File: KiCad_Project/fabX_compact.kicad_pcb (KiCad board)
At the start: 2 copper layers, 140.9 x 101.6 mm, 68 parts, among them J1 Conn_02x15_Odd_Even, J3 Conn_02x07_Odd_Even, J4 Conn_01x06, J6 Conn_01x08, Q1 2N7002, Q2 AO3401A, Q3 2N7002, Q4 2N7002, Q5 BCX19, Q6 BCX19, U1 MCP23008, U2 MCP23008

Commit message: some PCB progress
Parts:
- added J5: Conn_02x07_Odd_Even, Connector_IDC:IDC-Header_2x07_P2.54mm_Horizontal, F.Cu at (140.9, 96.8)
- added K2: FINDER-36.11-4301, Relay_THT:Relay_SPST_TE_PCN-1xxD3MHZ, F.Cu at (177.3, 121.7)
- added R22: 10k, Resistor_SMD:R_0603_1608Metric, F.Cu at (155.5, 79.8)
- added R23: 10k, Resistor_SMD:R_0603_1608Metric, F.Cu at (144.3, 79.8)
- added R24: 10k, Resistor_SMD:R_0603_1608Metric, F.Cu at (144.3, 78.2)
- C2: value C -> 100n 6v3 X7R
- D1, R10, R11, R12, R13, R14, R15, R16, R19, R9: moved to F.Cu
- D2, D3, D4, D5: moved to B.Cu
- JP4, JP5, JP6: value SolderJumper_3_Open -> SolderJumper_2_Open; footprint Jumper:SolderJumper-3_P1.3mm_Open_Pad1.0x1.5mm_NumberLabels -> Jumper:SolderJumper-2_P1.3mm_Open_RoundedPad1.0x1.5mm
- moved R1 143.7 mm to (214.1, 99.0), turned to 90 degrees
- moved H2 143.6 mm to (213.3, 130.6)
- moved Q2 140.1 mm to (212.3, 87.6), turned to 0 degrees
- moved R5 140.1 mm to (208.9, 99.0), turned to -90 degrees
- moved Q1 140.0 mm to (211.5, 99.0), turned to 0 degrees
- moved H1 139.7 mm to (216.1, 118.8)
- moved Q3 138.6 mm to (208.7, 87.6), turned to 0 degrees
- moved R6 138.0 mm to (208.9, 90.2), turned to 180 degrees
- moved R7 136.2 mm to (208.9, 85.0), turned to 0 degrees
- moved R14 135.9 mm to (212.1, 90.2)
- moved R15 134.8 mm to (212.1, 85.0)
- moved R19 117.2 mm to (168.3, 127.0)
- moved D1 114.7 mm to (170.3, 123.4)
- moved H3 114.2 mm to (226.9, 87.2)
- moved R8 111.6 mm to (167.5, 124.6)
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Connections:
- C2 pad 2: 5V -> +3V3
- J1 pad 10: /NFC_CS -> /NFC_IRQ
- J1 pad 19: /NFC_RST -> /NFC_CS
- J1 pad 20: /NFC_IRQ -> /NFC_RST
- J3 pad 10: /Ch3 -> /Ch4
- J3 pad 11: /Ch4 -> /Ch3
- J3 pad 12: /Ch5 -> /Ch2
- J3 pad 13: /Ch6 -> /Ch1
- J3 pad 14: /Ch7 -> /Ch0
- J3 pad 7: /Ch0 -> /Ch7
- J3 pad 8: /Ch1 -> /Ch6
- J3 pad 9: /Ch2 -> /Ch5
- JP4 pad 2: Net-(JP4-Pad2) -> Net-(U2-Pad5)
- JP5 pad 1: 5V -> GND
- JP6 pad 2: Net-(JP6-Pad2) -> Net-(U2-Pad3)
- U2 pad 12: In1 -> /Ch10
- U2 pad 13: In2 -> /Ch11
- U2 pad 14: In3 -> /Ch12
- U2 pad 15: In4 -> /Ch13
- U2 pad 16: In5 -> /Ch14
- U2 pad 17: In6 -> /Ch15
- U2 pad 18: In7 -> /Ch16
- U2 pad 19: unconnected-(U2-Pad19) -> /Ch17
- U2 pad 20: 5V -> +3V3
- U2 pad 3: Net-(JP4-Pad2) -> Net-(U2-Pad3)
- U2 pad 5: Net-(JP6-Pad2) -> Net-(U2-Pad5)
- U2 pad 6: 5V -> +3V3
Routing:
- net /NFC_CS: track 0.00 -> 86.7 mm, vias 0 -> 1
- net RX: track 20.0 -> 95.5 mm
- net TX: track 25.3 -> 88.8 mm
- net /coreRST: track 3.23 -> 65.4 mm, vias 0 -> 1
- net /COPI: track 17.7 -> 76.2 mm
- net /CIPO: track 19.0 -> 73.7 mm
- net /Fet1: track 53.8 -> 0.00 mm, vias 1 -> 0
- net GND: track 124.3 -> 72.0 mm, vias 9 -> 4
- net /SCLK: track 30.9 -> 82.0 mm
- net 3,3V: track 50.7 -> 0.00 mm
- net +3V3: track 35.4 -> 83.0 mm, vias 5 -> 0
- net /NFC_RST: track 36.9 -> 81.8 mm
- net /G0(BOOT): track 20.4 -> 57.6 mm, vias 2 -> 0
- net Net-(J6-Pad3): track 39.7 -> 2.59 mm
- net +5V: track 13.0 -> 49.5 mm, vias 2 -> 0
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- removed copper zone on B.Cu, net 5V
- removed copper zone on F.Cu, net GND
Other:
- board size 140.9 x 101.6 mm -> 62 x 90 mm
- board text removed: "3,3V, OUT4, OUT3, OUT2, OUT1 3,3V, GND, GND, GND, GND"
- board text removed: "5V"
- board text removed: "5V, OUT5, OUT6, OUT7, OUT8 5V, GND, GND, GND, GND"
- board text removed: ">"
- board text removed: "GND, IN7, IN5, IN3, IN1 GND, GND, IN6, IN4, IN2"
- board text removed: "MOSI, MISO, CLK, GND 3,3V, IO2, IO5, IO3"

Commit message: PCB progress
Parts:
- removed H1, H2: MountingHole_Pad, TestPoint:TestPoint_Loop_D2.50mm_Drill1.85mm
- removed kibuzzard-632A463E: G***, kibuzzard-632A463E
- removed kibuzzard-632A464C: G***, kibuzzard-632A464C
- removed kibuzzard-632A4658: G***, kibuzzard-632A4658
- removed kibuzzard-632A4688: G***, kibuzzard-632A4688
- removed kibuzzard-632A4693: G***, kibuzzard-632A4693
- removed kibuzzard-632A469F: G***, kibuzzard-632A469F
- added X2: Screw_Terminal_01x08, Connector_Phoenix_MSTB:PhoenixContact_MSTBA_2,5_8-G-5,08_1x08_P5.08mm_Horizontal, B.Cu at (167.7, 142.3)
- added kibuzzard-635FD364: G***, kibuzzard-635FD364, F.Cu at (128.0, 96.8)
- added kibuzzard-635FD36E: G***, kibuzzard-635FD36E, F.Cu at (128.0, 94.3)
- added kibuzzard-635FD378: G***, kibuzzard-635FD378, F.Cu at (128.0, 91.7)
- D2, D3, D4, D5: footprint LED_SMD:LED_0603_1608Metric -> LED_SMD:LED_1206_3216Metric_ReverseMount_Hole1.8x2.4mm; moved to F.Cu
- H10, H12, H13, H4, H6, H7: footprint MountingHole:MountingHole_3.2mm_M3 -> ownCon:MountingHole_3.2mm_M3_noSolder
- H11, H5, H8, H9: footprint MountingHole:MountingHole_3.2mm_M3 -> ownCon:MountingHole_3.2mm_M3_noSolderCorner
- K2: moved to B.Cu
- R16, R19: footprint Resistor_SMD:R_0603_1608Metric -> Resistor_SMD:R_2010_5025Metric
- moved H3 80.6 mm to (159.5, 131.4)
- moved R1 76.7 mm to (148.3, 138.5), turned to 0 degrees
- moved R14 75.2 mm to (154.4, 138.5)
- moved R6 75.1 mm to (151.3, 138.5)
- moved R7 74.7 mm to (151.9, 133.3)
- moved Q2 74.5 mm to (155.6, 135.9)
- moved Q3 74.5 mm to (152.0, 135.9)
- moved R15 74.5 mm to (155.4, 133.3)
- moved Q1 73.0 mm to (148.5, 135.9)
- moved R5 69.7 mm to (148.2, 133.3), turned to 0 degrees
- moved R9 55.6 mm to (125.5, 143.4), turned to 180 degrees
- moved D5 55.0 mm to (178.3, 119.5)
- moved R10 51.9 mm to (125.5, 140.0), turned to 180 degrees
- moved R12 48.3 mm to (125.5, 136.6), turned to 180 degrees
- moved R13 38.5 mm to (174.3, 120.2), turned to 0 degrees
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- renumbered JP1 to J1, JP2 to J2, JP3 to J3, JP4 to J4, JP5 to J5, JP6 to J6, J1 to X1, J3 to X3, J4 to X4, J5 to X5, J6 to X6
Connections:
- K2 pad 1: (no net) -> /Fet0
- K2 pad 2: (no net) -> +5V
- K2 pad 3: (no net) -> /Relay_COM
- K2 pad 4: (no net) -> /Relay_NO
- X4 pad 3: 3,3V -> +3V3
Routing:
- net +3V3: track 83.0 -> 219.6 mm, vias 0 -> 5
- net +5V: track 49.5 -> 169.0 mm
- net /Ch0: track 11.3 -> 116.1 mm, vias 0 -> 2
- net /Ch1: track 12.6 -> 100.0 mm, vias 0 -> 2
- net /Ch2: track 21.3 -> 98.2 mm, vias 0 -> 2
- net GND: track 72.0 -> 0.00 mm, vias 4 -> 28
- net /Relay_NO: track 0.00 -> 25.8 mm
- net /Fet0: track 0.00 -> 24.8 mm
- net /Relay_COM: track 0.00 -> 17.3 mm
- net /V_HIGH: track 0.00 -> 12.6 mm
- net /Fet2: track 0.00 -> 11.8 mm
- net /highOut: track 0.00 -> 9.79 mm
- net /Fet1: track 0.00 -> 7.09 mm
- net RX: track 95.5 -> 89.8 mm
- net TX: track 88.8 -> 83.4 mm
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- added copper zone on B.Cu, net GND
- added copper zone on F.Cu, net GND
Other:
- outline, holes or cut-outs redrawn
- board text added: "+3V3"
- board text added: "+5V"
- board text added: "COM"
- board text added: "CTS"
- board text added: "Ch. 0-7"
- board text added: "Ch. 10-17"
- board text added: "Ch0"
- board text added: "Ch1"
- board text added: "Ch2"
- board text added: "DTR"
- board text added: "GND"
- board text added: "LOut"
- board text added: "NO"
- board text added: "Nylon Screw only"
- board text added: "PWR"
- board text added: "RX"
- board text added: "TX"
- board text added: "V- High"
- board text added: "fabX FabLab München compact V0.1 @tinyledmatrix 2022-10-24"
- board text added: "hOut"
- board text removed: "fabX FabLab München compact V0.1 @tinyledmatrix 2022-09-21"

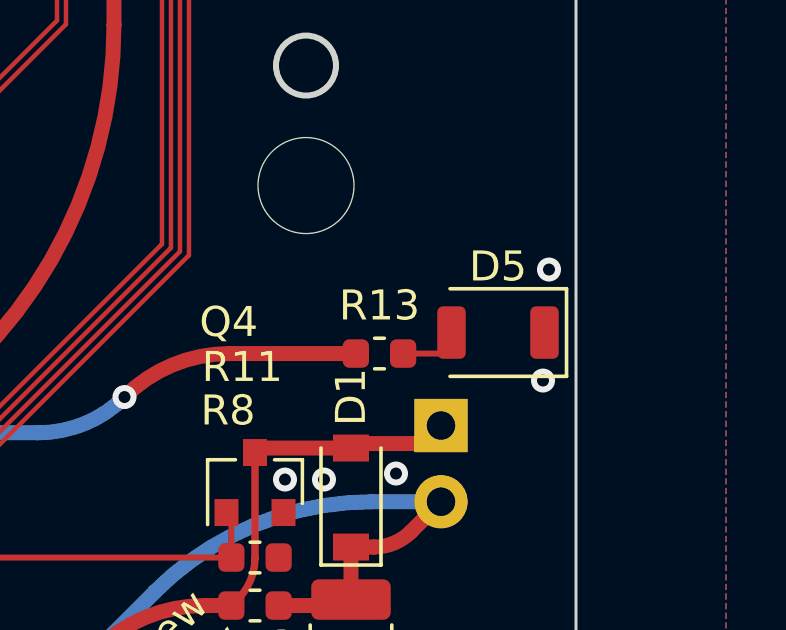
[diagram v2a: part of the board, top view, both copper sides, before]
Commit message: added bom
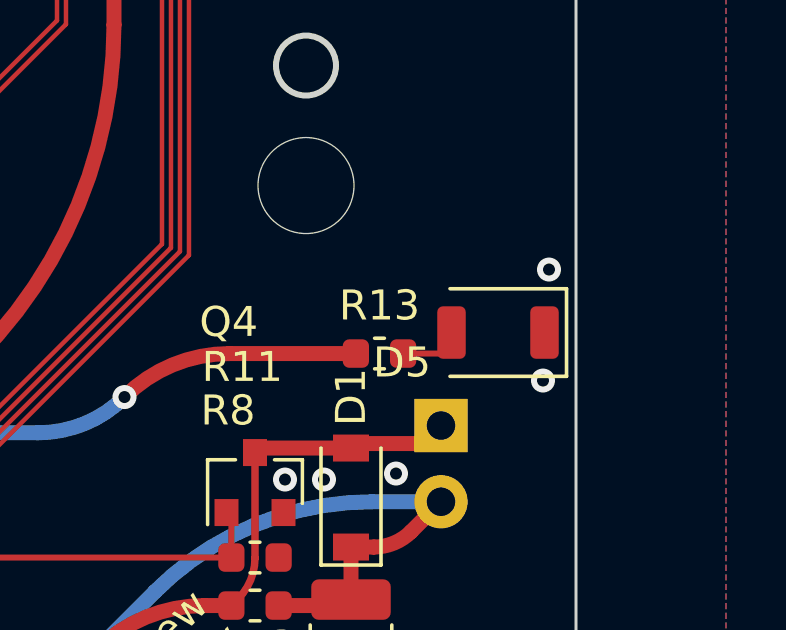
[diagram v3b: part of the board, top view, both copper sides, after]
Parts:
- D2, D3, D4, D5: footprint LED_SMD:LED_1206_3216Metric_ReverseMount_Hole1.8x2.4mm -> ownLEDs:LED_1206_3216Metric_ReverseMount_Hole1.8x2.4mm_3DMOD
- K2: value FINDER-36.11-4301 -> PCN-105D3MHZ
- Q2: value AO3401A -> DMP3056L-7
